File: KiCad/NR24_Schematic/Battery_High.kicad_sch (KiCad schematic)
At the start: 9 parts

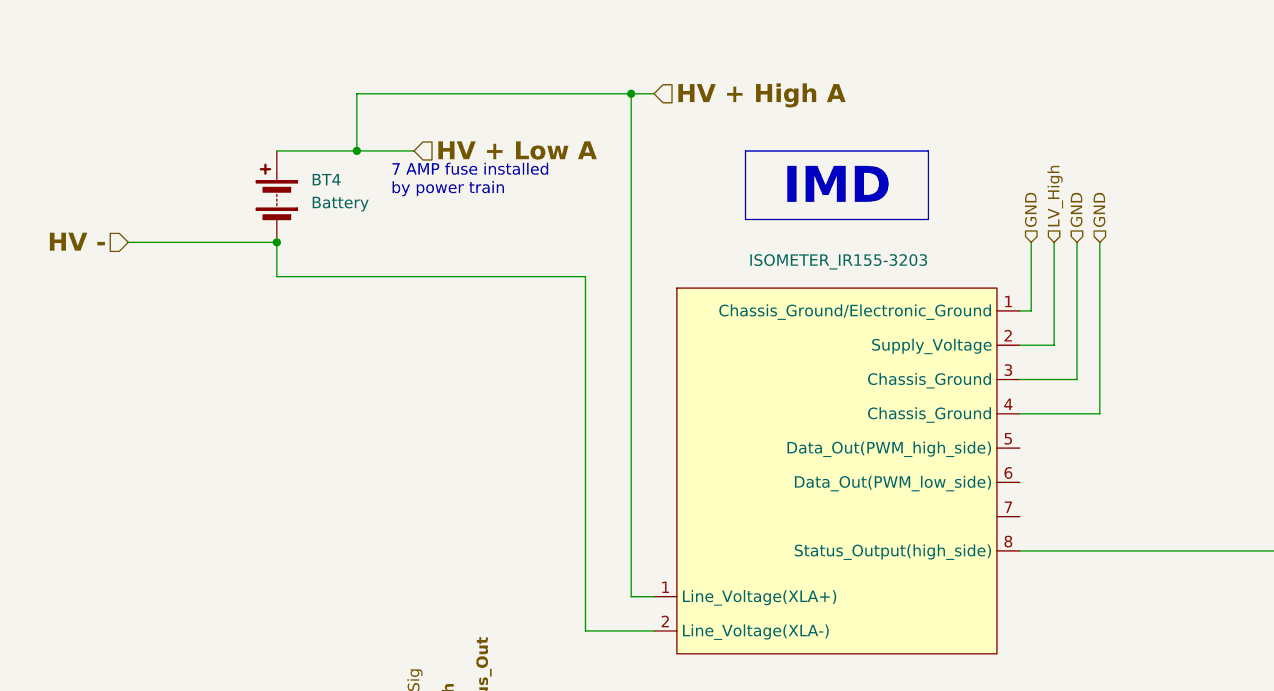
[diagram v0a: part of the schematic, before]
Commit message: Changed IMD, added NR24 library
I changed the IMD from the IR155 to the iso175, and created a symbol library to hold the team's symbols.
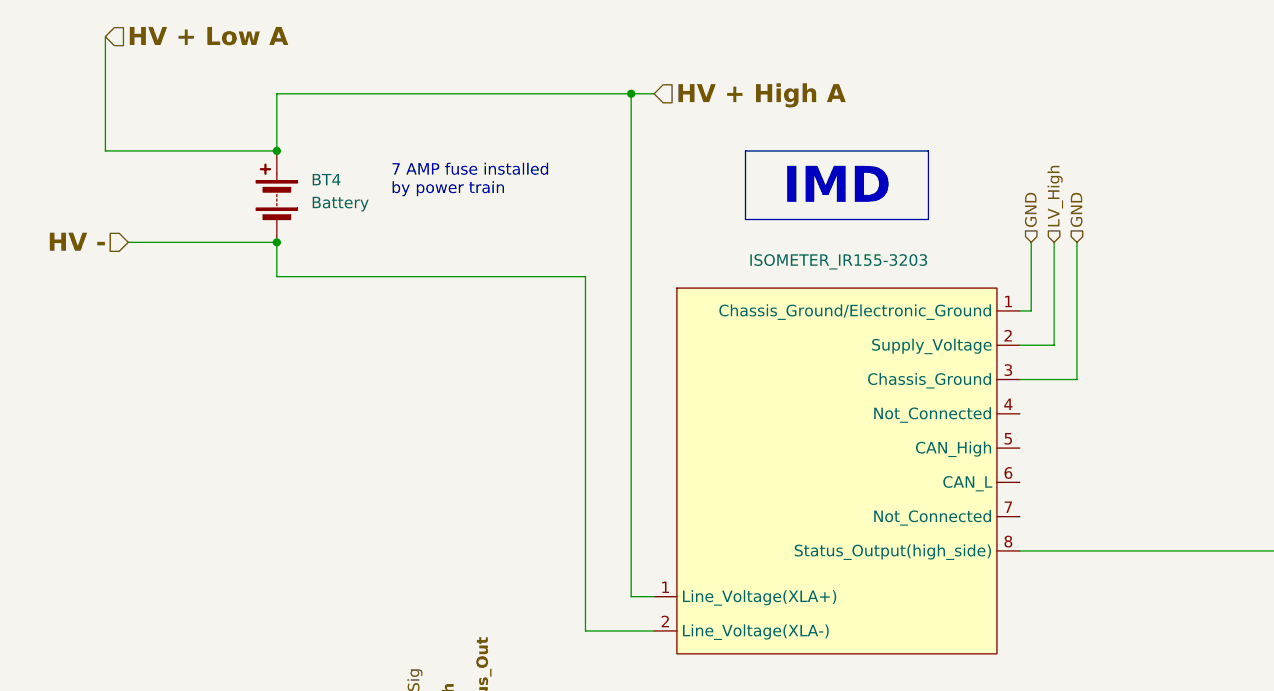
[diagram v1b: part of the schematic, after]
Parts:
- U?: symbol CamachosSymbols:Sevcon_Gen4_Size6 -> NR24:ISOMETER_iso175C-32-SS
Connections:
- net GND: no longer U?.4 (Chassis_Ground)
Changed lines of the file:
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@@
 (kicad_sch (version 20230121) (generator eeschema)
   (paper "A4")
+  (junction (at 78.74 38.1) (diameter 0) (color 0 0 0 0)
+  )
   (junction (at 118.11 31.75) (diameter 0) (color 0 0 0 0)
-  )
-  (junction (at 87.63 38.1) (diameter 0) (color 0 0 0 0)
   )
   (junction (at 210.82 82.55) (diameter 0) (color 0 0 0 0)
@@
     (stroke (width 0) (type default))
   )
-  (wire (pts (xy 87.63 31.75) (xy 118.11 31.75))
+  (wire (pts (xy 78.74 31.75) (xy 118.11 31.75))
     (stroke (width 1) (type default))
   )
@@
     (stroke (width 1) (type default))
   )
+  (wire (pts (xy 59.69 38.1) (xy 78.74 38.1))
+    (stroke (width 1) (type default))
+  )
   (wire (pts (xy 233.68 78.74) (xy 231.14 78.74))
     (stroke (width 0) (type default))
@@
     (stroke (width 0) (type default))
   )
-  (wire (pts (xy 87.63 38.1) (xy 87.63 31.75))
+  (wire (pts (xy 78.74 38.1) (xy 78.74 31.75))
     (stroke (width 1) (type default))
   )
@@
     (stroke (width 0) (type default))
   )
+  (wire (pts (xy 59.69 25.4) (xy 59.69 38.1))
+    (stroke (width 1) (type default))
+  )
   (wire (pts (xy 104.14 124.46) (xy 118.11 124.46))
     (stroke (width 0) (type default))
@@
     (stroke (width 0) (type default))
   )
-  (wire (pts (xy 170.18 48.26) (xy 170.18 67.31))
-    (stroke (width 0) (type default))
-  )
   (wire (pts (xy 231.14 45.72) (xy 233.68 45.72))
     (stroke (width 0) (type default))
   )
   (wire (pts (xy 167.64 48.26) (xy 167.64 63.5))
-    (stroke (width 0) (type default))
-  )
-  (wire (pts (xy 161.29 67.31) (xy 170.18 67.31))
     (stroke (width 0) (type default))
   )
@@
     (stroke (width 0) (type default))
   )
-  (wire (pts (xy 78.74 38.1) (xy 87.63 38.1))
-    (stroke (width 1) (type default))
-  )
-  (wire (pts (xy 87.63 38.1) (xy 93.98 38.1))
-    (stroke (width 1) (type default))
-  )
   (wire (pts (xy 172.72 149.86) (xy 210.82 149.86))
     (stroke (width 0) (type default))
@@
     (effects (font (size 1.27 1.27)) (justify left))
   )
-  (hierarchical_label "GND" (shape input) (at 170.18 48.26 90) (fields_autoplaced)
-    (effects (font (size 1.27 1.27)) (justify left))
-  )
   (hierarchical_label "GND" (shape input) (at 251.46 113.03 0) (fields_autoplaced)
     (effects (font (size 1.27 1.27)) (justify left))
@@
     (effects (font (size 1.27 1.27)) (justify left))
   )
-  (hierarchical_label "HV + Low A" (shape input) (at 93.98 38.1 0) (fields_autoplaced)
+  (hierarchical_label "HV + Low A" (shape input) (at 59.69 25.4 0) (fields_autoplaced)
     (effects (font (size 2 2) (thickness 0.4) bold) (justify left))
   )
@@
     )
   )
-  (symbol (lib_name "Sevcon_Gen4_Size6_1") (lib_id "CamachosSymbols:Sevcon_Gen4_Size6") (at 140.97 67.31 0) (unit 1)
+  (symbol (lib_id "NR24:ISOMETER_iso175C-32-SS") (at 140.97 67.31 0) (unit 1)
     (in_bom yes) (on_board yes) (dnp no)
     (property "Reference" "U?" (at 130.81 49.53 0)
